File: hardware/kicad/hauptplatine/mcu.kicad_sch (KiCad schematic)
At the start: 33 parts, among them J301 USB-C, J302 Debug (SWD + Serial1), SW301 Reset, SW302 BOOT, SW303 Service, SW304 MRS03-B-3, U301 STM32F411CEU6, U302 USBLC6-2SC6, Y301 25MHz 12pF, Y302 32,768k 7pF

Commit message: HW-09: BLE-Modul RN4871 an USART6 statt USB-Daten, USB-C nur Laden
Warum: Service-Zugang ohne Öffnen des Gehäuses (Lastenheft F7); Vorschlagspaket
„USB → BLE RN4871“ vom 18.10.2026 geprüft und eingearbeitet (Pinwahl USART6
PA11/PA12 bestätigt, Modul übernommen; Versorgung, Reset und USB-Laden anders).

Was:
- Blatt MCU: U303 RN4871-I/RM130 (C633942) an USART6 über R310/R311 1 kΩ;
  Lastschalter Q301 AO3401A an PB13 (low = ein, R309 100k), C314/C315 an VBAT,
  R312 10k (P2_0) an BLE_VCC, C316 an RST_N, JP301 „BLE dauernd“, #FLG302.
- USB-C J301 nur Laden: D+/D− offen, U302 und R307/R308 entfernt (SCH26-10
  gegenstandslos). J704 Pin 9–11 = BLE_RXD/BLE_TXD/BLE_MODE.
- Symbol Bienen:RN4871 (DS50002489D Tab. 1-2), Footprint Bienen:Microchip_RN4871
  mit Sperrzonen (Antenne *.Cu, Testpunkte F.Cu) nach Fig. 4-7/4-8 [A].
- netz_tests.py: ble() mit Gegenprobe, J704/J11, USB ohne Daten;
  pin_footprint.py: RN4871 [V], AO3401A.
- Dokumente: mcu-funk.md 1.3/1.6, Lastenheft K5/K6/F9/M5/M8, anschluesse.md,
  versorgung.md, energiebilanz.py (2a BLE-Sitzung), Pflichtenheft/Fiverr,
  KiCad-README, Entscheidungsregister HW-09, Befundregister HW26-20, CHANGELOG,
  Bericht docs/testberichte/2026-10-18-hw09-ble-rn4871.md.

Offen (Philipp): USB-C-Buchse als Ladebuchse behalten (umgesetzt) oder entfernen.

Tests (T0/T3, KiCad 10.0.7 Windows): pruefen.sh reproduzierbar, ERC 0,
Netzprüfung 220/220, Pin/Footprint 179/0; energiebilanz.py, i2c_leitung.py,
netz_vergleich.py --selbsttest ok. Keine Messung, keine BLE-Firmware;
alle_tests_linux.sh nicht lokal gelaufen (CI).

Co-Authored-By: Claude Fable 5.1 <noreply@anthropic.com>
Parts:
- removed R307: 33k, Resistor_SMD:R_0603_1608Metric, symbol Device:R
- removed R308: 82k, Resistor_SMD:R_0603_1608Metric, symbol Device:R
- removed U302: USBLC6-2SC6, Package_TO_SOT_SMD:SOT-23-6, symbol Power_Protection:USBLC6-2SC6
- added C314: 10µ 6,3V X5R, Capacitor_SMD:C_0805_2012Metric, symbol Device:C
- added C315, C316: 100n, Capacitor_SMD:C_0603_1608Metric, symbol Device:C
- added JP301: BLE dauernd, Jumper:SolderJumper-2_P1.3mm_Open_RoundedPad1.0x1.5mm, symbol Jumper:SolderJumper_2_Open
- added Q301: AO3401A, Package_TO_SOT_SMD:SOT-23, symbol Transistor_FET:AO3401A
- added R309: 100k, Resistor_SMD:R_0603_1608Metric, symbol Device:R
- added R310, R311: 1k, Resistor_SMD:R_0603_1608Metric, symbol Device:R
- added R312: 10k, Resistor_SMD:R_0603_1608Metric, symbol Device:R
- added U303: RN4871-I/RM130, Bienen:Microchip_RN4871, symbol Bienen:RN4871
- J301: value USB-C -> USB-C (nur Laden)
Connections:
- net +3V3: now also JP301.2 (B), Q301.2 (S), R309.1
- net GND: now also C314.2, C315.2, C316.2, U303.13 (GND), U303.2 (GND)
- removed net USB_DM: J301.A7 (D-), J301.B7 (D-), U301.32 (PA11)
- removed net USB_DP: J301.A6 (D+), J301.B6 (D+), U301.33 (PA12)
- net VBUS_SENSE renamed BLE_EIN
- net BLE_EIN: now also Q301.1 (G), R309.2
- new net BLE_MODE: R312.2, U303.16 (P2_0)
- new net BLE_RST: C316.1, U303.10 (RST_N)
- new net BLE_RXD: R310.2, U303.7 (UART_RX)
- new net BLE_TXD: R311.2, U303.8 (UART_TX)
- new net BLE_VCC: C314.1, C315.1, JP301.1 (A), Q301.3 (D), R312.1, U303.14 (VBAT)
- new net USART6_RX: R311.1, U301.33 (PA12)
- new net USART6_TX: R310.1, U301.32 (PA11)
- no-connect marks 2 -> 15
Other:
- note added: "4 USB-C nur zum Laden (HW-09): VBUS → D203 → Lader; D+/D− offen"
- note added: "5 Debug-Leiste: SWD und Serial1 (auch ROM-Bootloader über USART1)"
- note added: "6 BLE-Modul RN4871 (HW-09)"
- note added: "Firmware: PA11/PA12 bei abgeschaltetem Modul hochohmig, sonst Rückspeisung über die Modul-Schutzdioden"
- note added: "Modul-UART und P2_0 auch an J704 Pin 9–11 (Modul-Firmware-Update: JP301 zu, Pin 11 an GND, MCU in Reset)"
- note added: "Versorgung über Q301 aus +3V3, PB13 low = ein (Ruhestrom 0); UART an USART6 PA11/PA12 (AF8) über 1 kΩ"
- note removed: "4 USB-C (Aufspielen, Laden am Tisch) mit ESD-Schutz"
- note removed: "5 Debug-Leiste: SWD und Serial1"
- title: MCU: STM32F411CEU6, Takt, USB-C, Debug, Magnet und LED -> MCU: STM32F411CEU6, Takt, USB-C (Laden), BLE RN4871, Debug, Magnet und LED

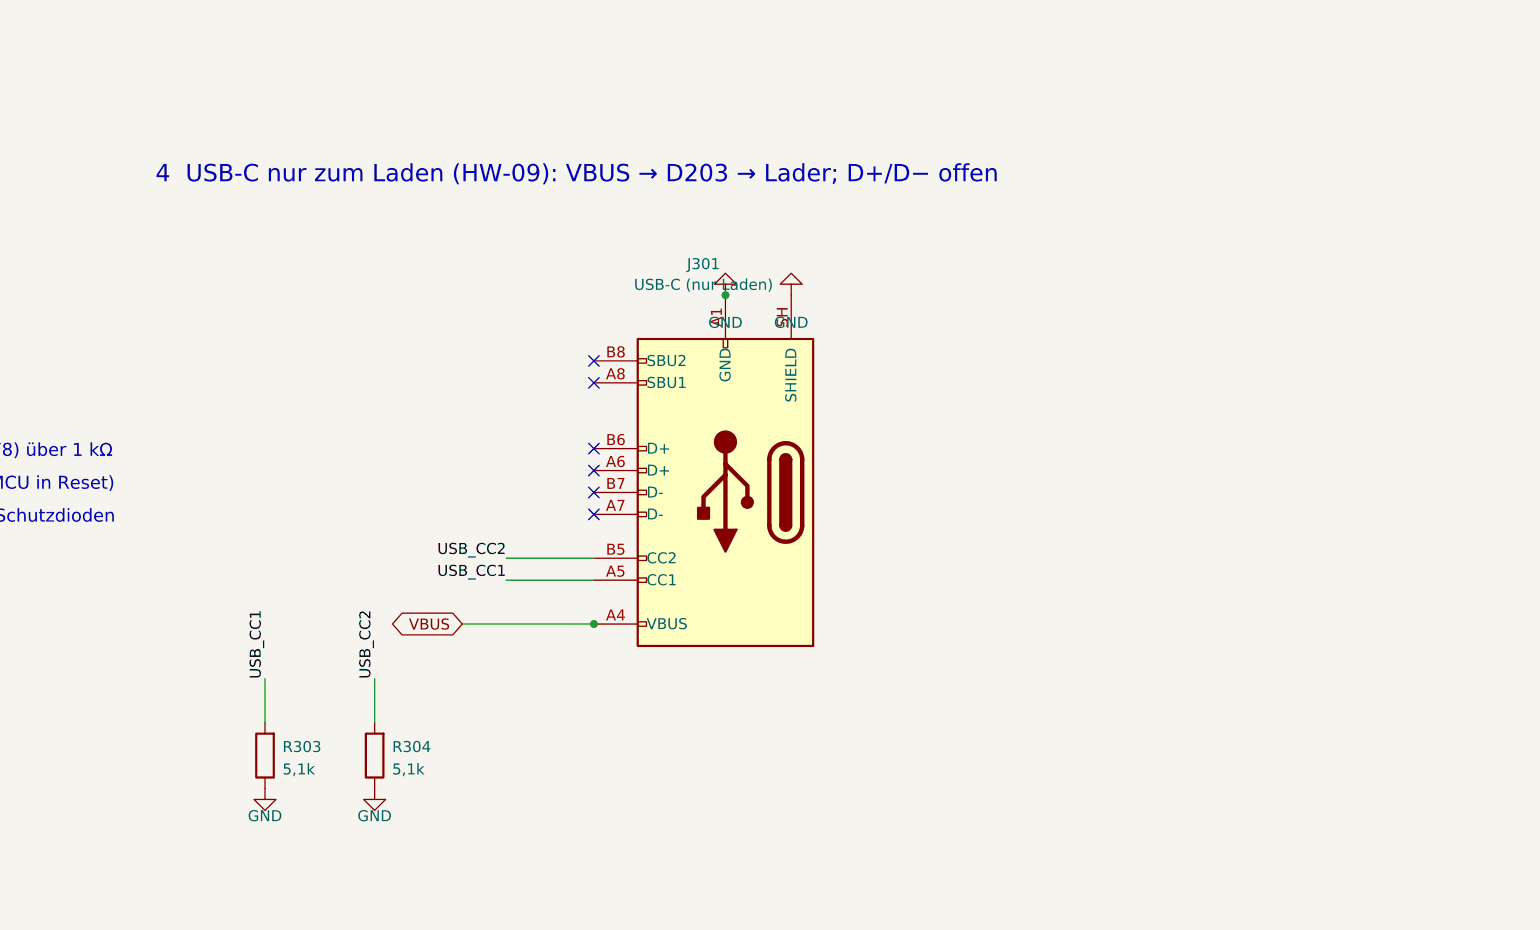
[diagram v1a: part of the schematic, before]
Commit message: HW-09: USB-C-Buchse entfaellt, Laden ueber zwei Pads J301 (Entscheidung Philipp)
J301 jetzt Conn_01x02 DNP (1 GND, 2 +5 V -> D203), R303/R304 entfernt; anschluesse.md J9 neu,
netz_tests.py prueft J9 gegen das Dokument, VBUS nur Pad 2 + D203, kein U302/R303/R304/R307/R308;
pin_footprint.py ohne USB. Dokumente: mcu-funk.md 1.3, Lastenheft K5/M5/M8, Pflichtenheft 4,
Fiverr (177 Teile), Entscheidungsregister HW-09 (Teilentscheid getroffen), Befundregister HW26-20,
CHANGELOG, KiCad-README (Stueckliste 177), Bericht (Nachtrag).
pruefen.sh: reproduzierbar, ERC 0, Netzpruefung 220/220, Pin/Footprint 177/0.

Co-Authored-By: Claude Fable 5.1 <noreply@anthropic.com>
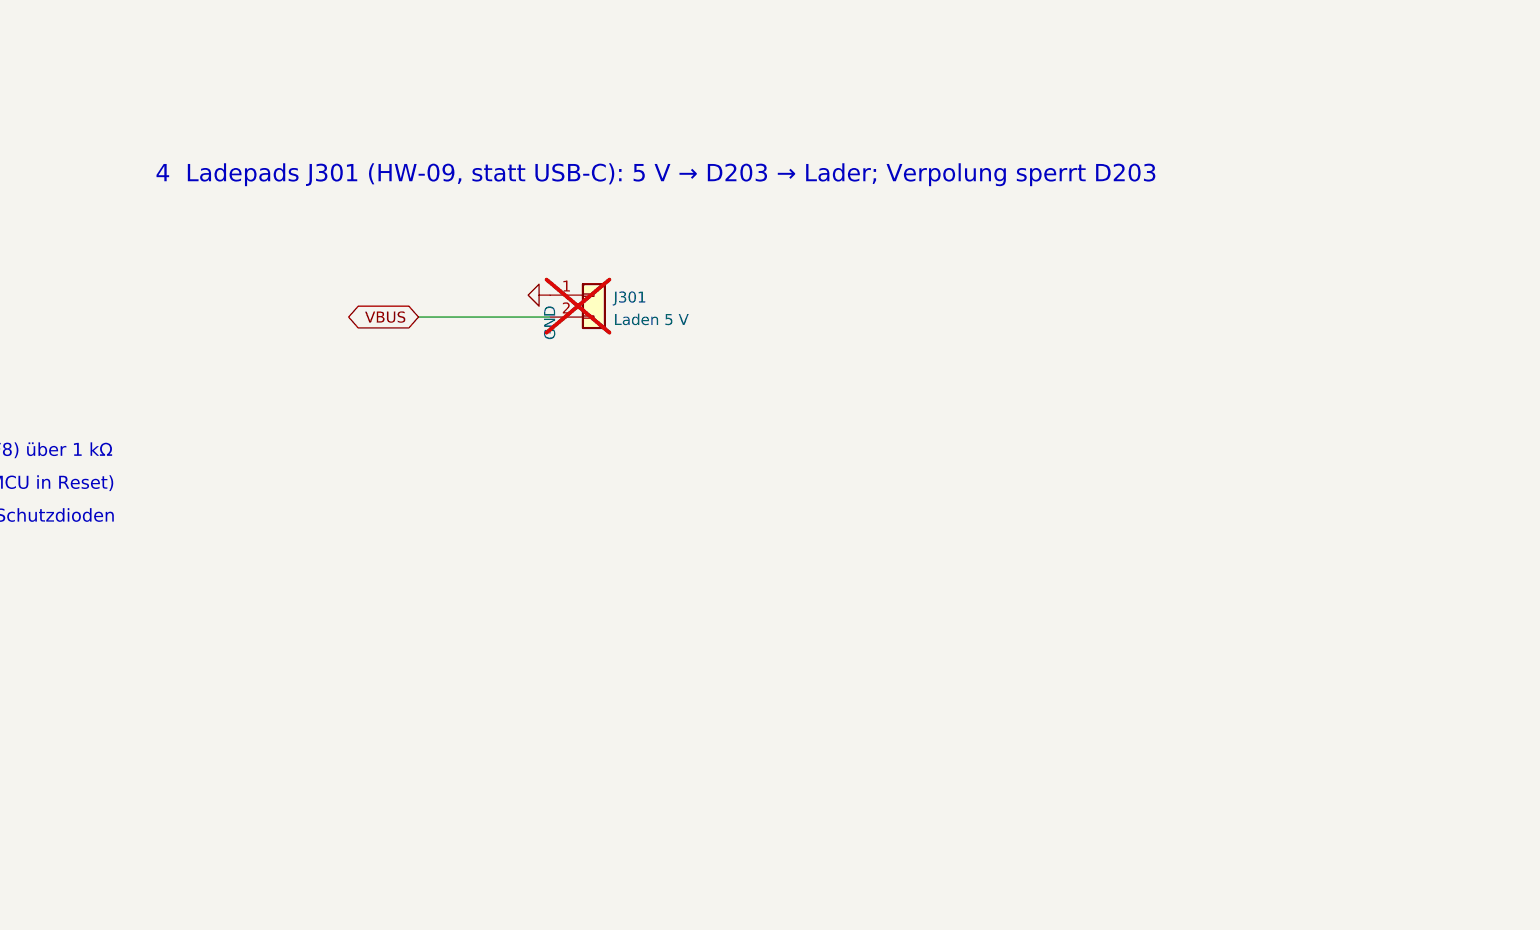
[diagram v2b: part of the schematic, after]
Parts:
- removed R303, R304: 5,1k, Resistor_SMD:R_0603_1608Metric, symbol Device:R
- J301: value USB-C (nur Laden) -> Laden 5 V; footprint Connector_USB:USB_C_Receptacle_HRO_TYPE-C-31-M-12 -> Connector_PinHeader_2.54mm:PinHeader_1x02_P2.54mm_Vertical; symbol Connector:USB_C_Receptacle_USB2.0_16P -> Connector_Generic:Conn_01x02; LCSC C165948 -> (none); now not fitted
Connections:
- net GND: now also J301.1 (Pin_1); no longer J301.A1 (GND), J301.A12 (GND), J301.B1 (GND), J301.B12 (GND), J301.SH (SHIELD)
- net VBUS: now also J301.2 (Pin_2); no longer J301.A4 (VBUS), J301.A9 (VBUS), J301.B4 (VBUS), J301.B9 (VBUS)
- removed net USB_CC1: J301.A5 (CC1)
- removed net USB_CC2: J301.B5 (CC2)
- no-connect marks 15 -> 9
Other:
- note added: "4 Ladepads J301 (HW-09, statt USB-C): 5 V → D203 → Lader; Verpolung sperrt D203"
- note removed: "4 USB-C nur zum Laden (HW-09): VBUS → D203 → Lader; D+/D− offen"
- title: MCU: STM32F411CEU6, Takt, USB-C (Laden), BLE RN4871, Debug, Magnet und LED -> MCU: STM32F411CEU6, Takt, Ladepads, BLE RN4871, Debug, Magnet und LED
